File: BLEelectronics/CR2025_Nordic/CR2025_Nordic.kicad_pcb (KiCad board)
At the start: 2 copper layers, 40.7 x 31.3 mm, 35 parts, among them IC1 LTC4412xS6, IC2 PCF8523T, IC3 MX25R6435FM2IL0, IC4 LTC4054LES5-4.2#TRPBF, J1 Nordic_nRF52840_breakout, J4 Conn_01x01_Female, Q1 Si2307CDS, Q2 Si7463DP, U1 LP5907MFX-3.3, U2 BAT-HLD-001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

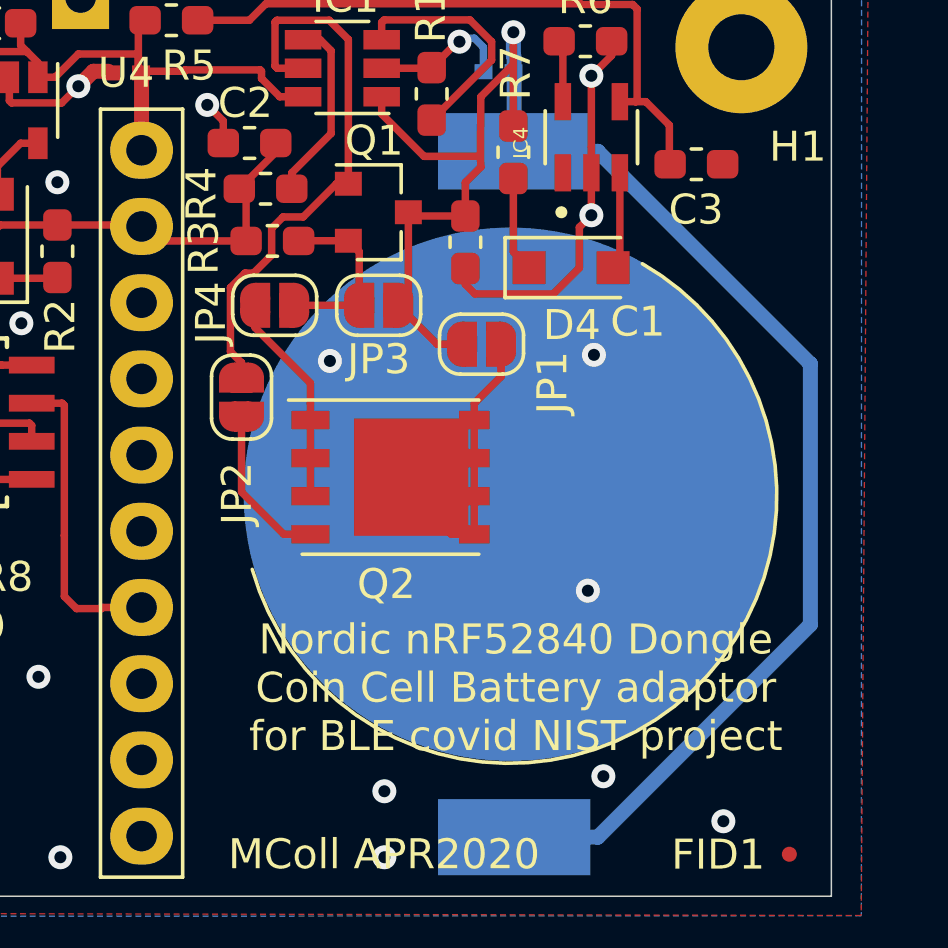
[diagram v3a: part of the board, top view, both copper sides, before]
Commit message: Expensive samsung capacitor removed
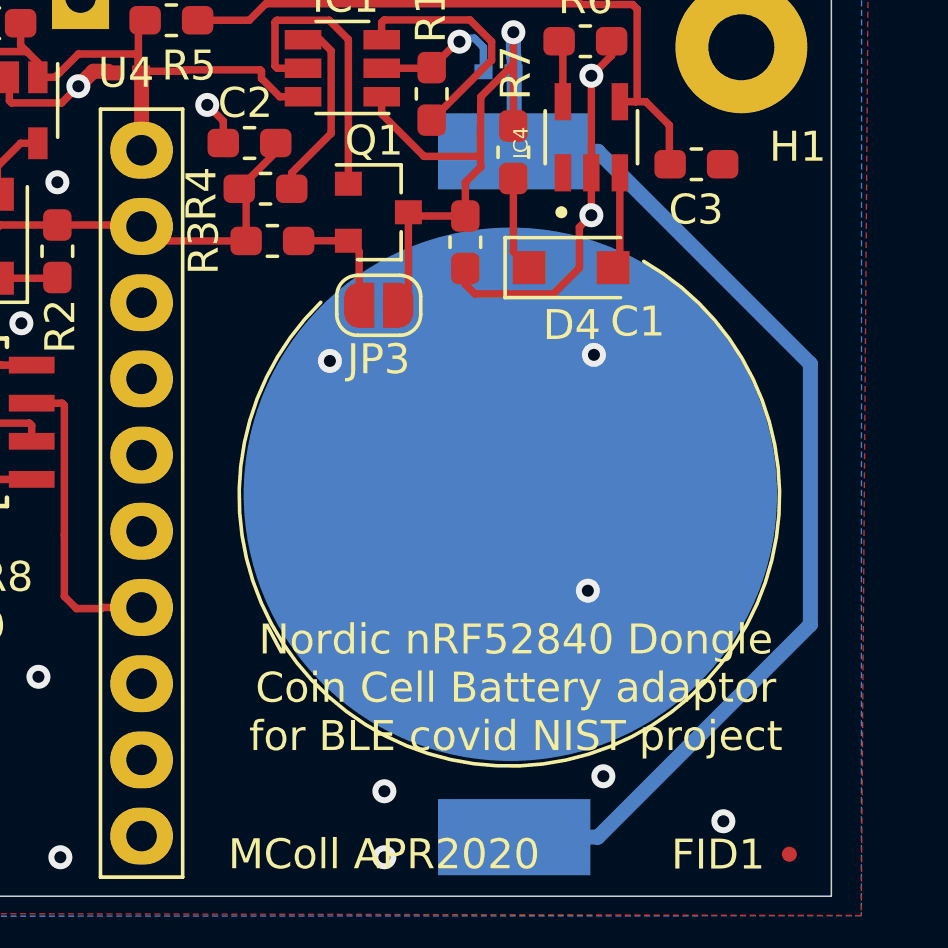
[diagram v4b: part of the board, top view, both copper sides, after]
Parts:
- removed JP1, JP2, JP4: Jumper_2_Open, Jumper:SolderJumper-2_P1.3mm_Open_RoundedPad1.0x1.5mm
- removed Q2: Si7463DP, Package_SO:PowerPAK_SO-8_Single
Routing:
- net Net-(JP1-Pad1): track 9.93 -> 0.00 mm
- net Net-(IC1-Pad5): track 19.0 -> 9.97 mm
- net Net-(JP4-Pad1): track 7.13 -> 0.00 mm
- net Net-(JP2-Pad2): track 5.39 -> 0.00 mm
- net /3V: track 59.7 -> 57.1 mm
- net Net-(JP3-Pad2): track 6.13 -> 3.96 mm

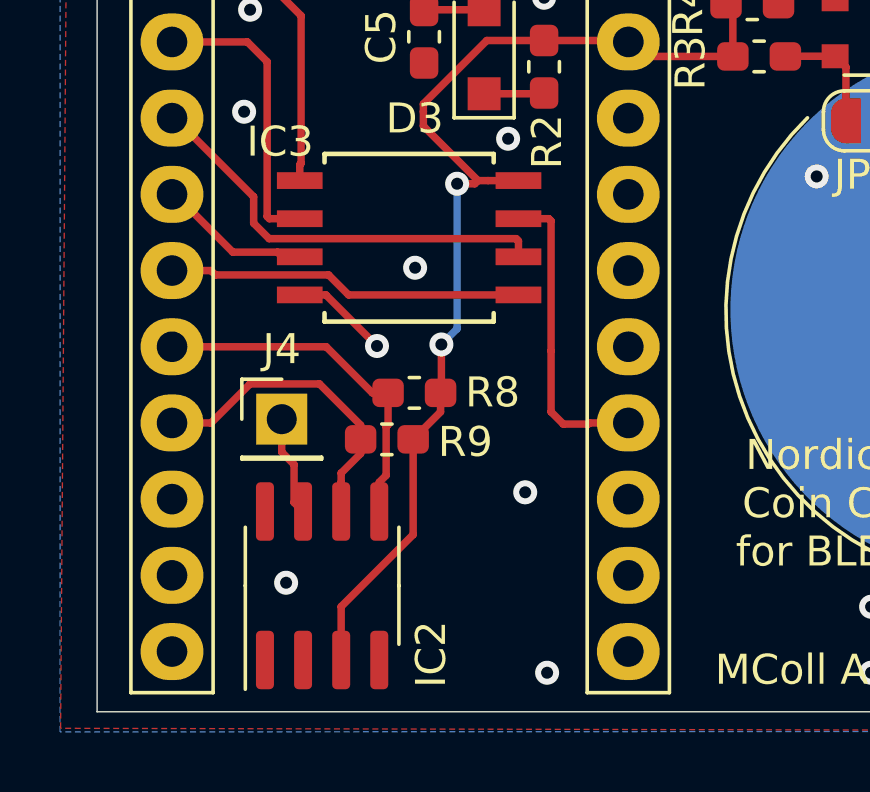
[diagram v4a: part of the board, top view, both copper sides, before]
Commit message: Moved power from pin 3 VBat to pin 8 Vdd on RTC. Swapped SIO3 and SDA on 1a and 1b. Changed battery footprint to allow backside routing for Flash and USB data. Todo: Unbreak MVP1B layout rerouting.
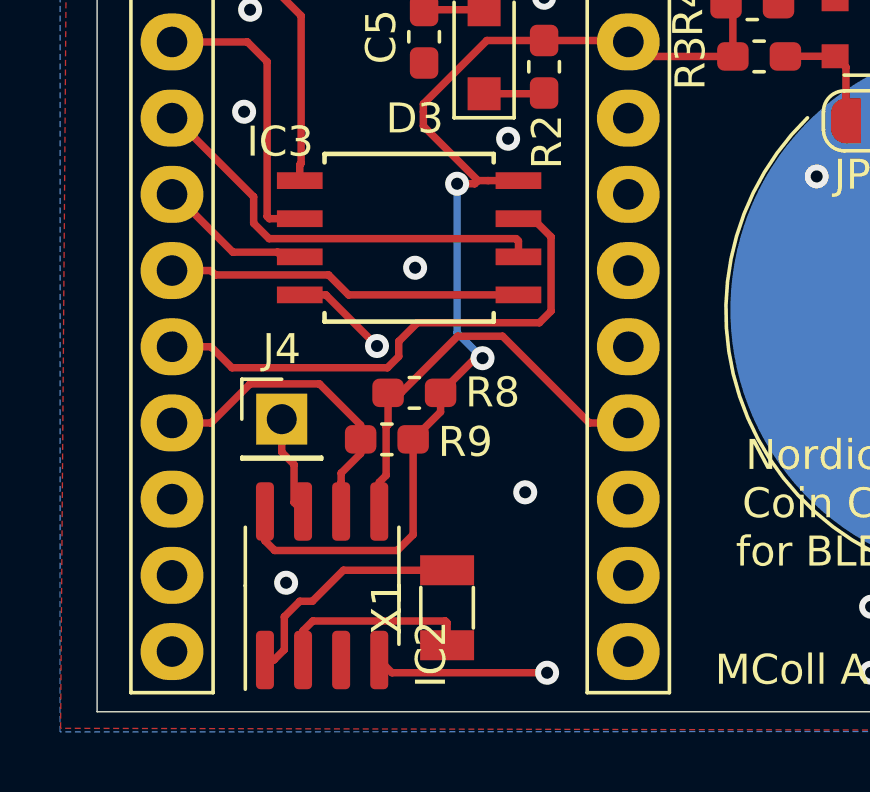
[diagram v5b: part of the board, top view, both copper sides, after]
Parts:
- added X1: 32.768KHZ, Crystal:Crystal_SMD_3215-2Pin_3.2x1.5mm, F.Cu at (136.0, 100.5)
- R8, R9: value 4.7K -> 10K
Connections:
- IC2 pad 3: /VDD_3V -> Net-(IC2-Pad3)
- IC2 pad 8: Net-(IC2-Pad8) -> /VDD_3V
- J1 pad 14: /RESET -> /SDA
- J1 pad 6: /SDA -> /RESET
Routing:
- net Net-(IC2-Pad1): track 0.00 -> 7.95 mm
- net /RESET: track 10.3 -> 17.9 mm
- net Net-(IC2-Pad2): track 0.00 -> 6.68 mm
- net GND: track 26.9 -> 32.6 mm
- net /SDA: track 12.0 -> 14.1 mm
- net /VDD_3V: track 38.2 -> 40.2 mm

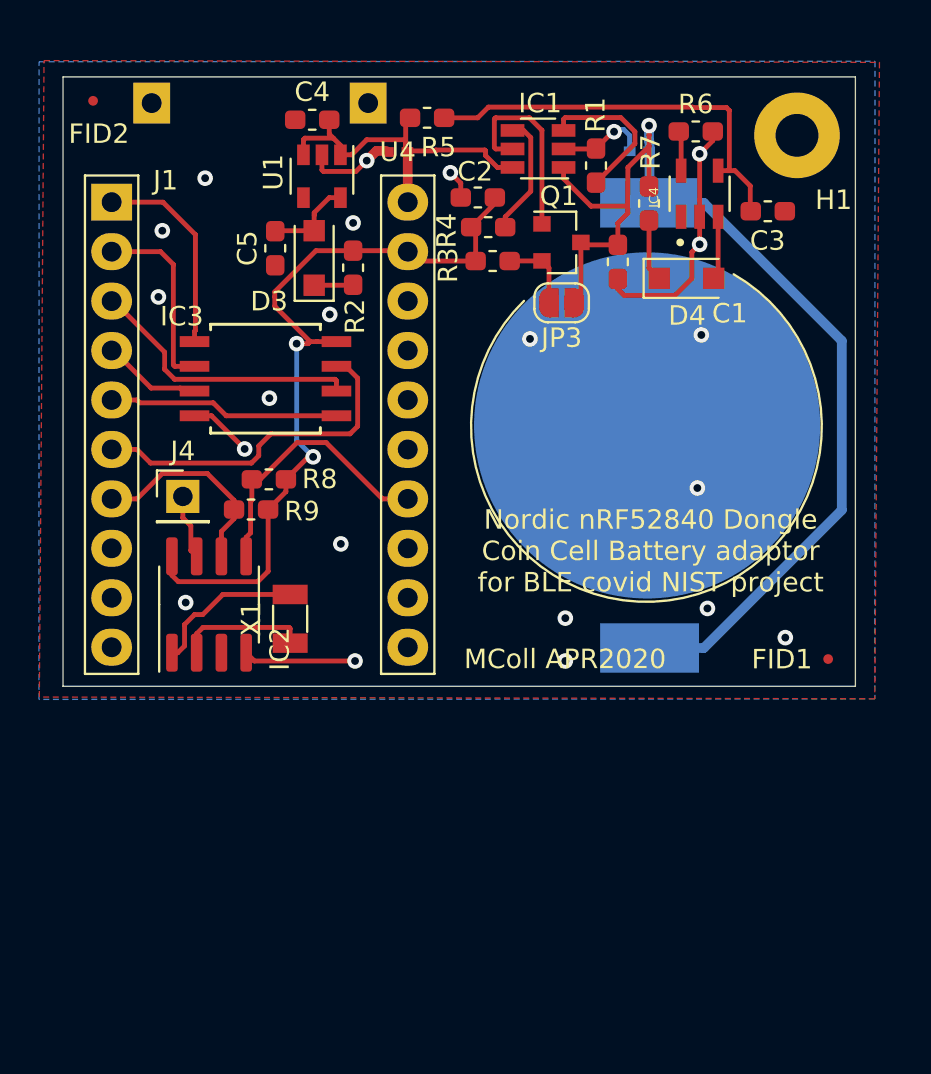
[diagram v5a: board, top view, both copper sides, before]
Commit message: refactored the MVP 1a to single sided form factor.
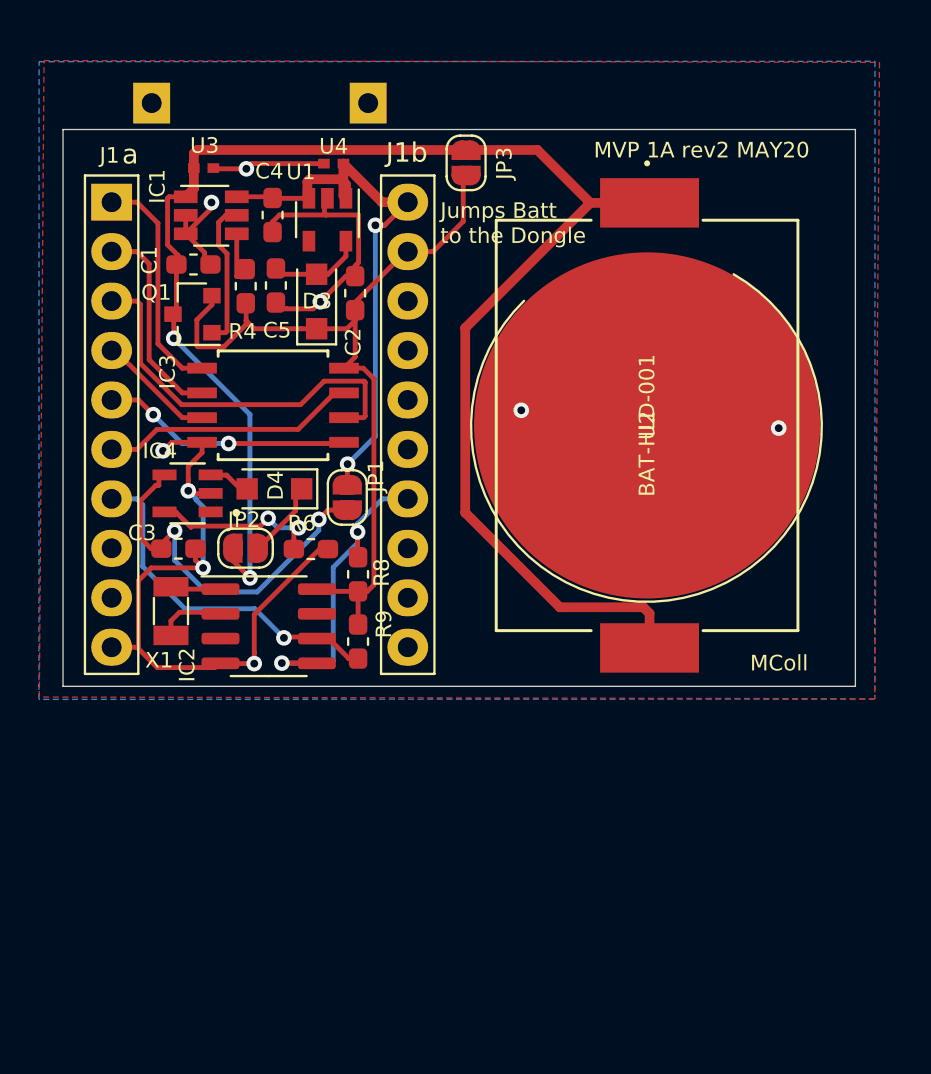
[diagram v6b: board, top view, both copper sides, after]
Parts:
- removed FID1, FID2: Fiducial, Fiducial:Fiducial_0.5mm_Mask1mm
- removed H1: MountingHole, MountingHole:MountingHole_2.2mm_M2_Pad
- removed J4: Conn_01x01_Female, Connector_PinHeader_2.54mm:PinHeader_1x01_P2.54mm_Vertical
- removed R1, R2, R3, R5, R7: 0, Resistor_SMD:R_0603_1608Metric_Pad1.05x0.95mm_HandSolder
- added JP1: Jumper_2_Open, Jumper:SolderJumper-2_P1.3mm_Open_RoundedPad1.0x1.5mm, F.Cu at (138.9, 94.3)
- added JP2: Jumper_2_Open, Jumper:SolderJumper-2_P1.3mm_Open_RoundedPad1.0x1.5mm, F.Cu at (133.7, 96.9)
- U2, U3: moved to F.Cu
- moved C3 34.9 mm to (130.2, 96.9)
- moved IC4 30.5 mm to (130.7, 94.1), turned to 180 degrees
- moved R6 29.2 mm to (137.0, 97.0)
- moved D4 23.8 mm to (135.2, 93.9), turned to 180 degrees
- moved U3 22.4 mm to (131.5, 77.4), turned to 180 degrees
- moved C1 21.8 mm to (131.0, 82.3), turned to 0 degrees
- moved Q1 19.3 mm to (130.9, 84.9), turned to 180 degrees
- moved IC1 17.1 mm to (131.9, 79.8), turned to 0 degrees
- moved R4 12.8 mm to (133.7, 83.4), turned to 90 degrees
- moved R9 8.73 mm to (139.5, 101.7), turned to 270 degrees
- moved JP3 8.70 mm to (145.0, 77.1), turned to 270 degrees
- moved C2 7.99 mm to (139.3, 83.8), turned to 90 degrees
- moved R8 6.69 mm to (139.5, 98.2), turned to 90 degrees
- moved X1 6.13 mm to (129.8, 100.1)
- moved C4 5.30 mm to (135.1, 79.8), turned to 90 degrees
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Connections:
- D3 pad 1: Net-(D3-Pad1) -> /VDD_3V
- IC1 pad 3: Net-(IC1-Pad3) -> GND
- JP3 pad 2: Net-(JP3-Pad2) -> /VDD_3V
- Q1 pad 2: Net-(JP3-Pad2) -> /VDD_3V
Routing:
- net GND: track 32.6 -> 59.4 mm, vias 22 -> 9
- net /3V: track 57.1 -> 83.3 mm, vias 1 -> 2
- net /5Vusb: track 19.1 -> 30.3 mm, vias 0 -> 2
- net Net-(IC1-Pad3): track 8.02 -> 0.00 mm
- net Net-(IC4-Pad5): track 1.80 -> 9.56 mm, vias 0 -> 2
- net /SCL: track 10.5 -> 18.0 mm, vias 0 -> 1
- net /SCLK: track 14.3 -> 20.4 mm
- net Net-(IC2-Pad1): track 7.95 -> 2.65 mm
- net /RESET: track 17.9 -> 13.2 mm
- net Net-(JP3-Pad2): track 3.96 -> 0.00 mm
- net Net-(IC1-Pad4): track 6.23 -> 2.67 mm
- net /VDD_3V: track 40.2 -> 43.7 mm, vias 2 -> 0
- net Net-(IC2-Pad7): track 3.37 -> 0.00 mm
- net Net-(IC2-Pad2): track 6.68 -> 3.48 mm
- net /SDA: track 14.1 -> 16.6 mm, vias 0 -> 2
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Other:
- board size 40.7 x 31.3 mm -> 40.7 x 28.6 mm
- board text added: "J1b"
- board text added: "Jumps Batt to the Dongle"
- board text added: "MColl"
- board text added: "MVP 1A rev2 MAY20"
- board text added: "a"
- board text removed: "MColl APR2020"
- board text removed: "Nordic nRF52840 Dongle Coin Cell Battery adaptor for BLE covid NIST project"

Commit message: generated gerber files for JLC order 07MAy20 of MVP-1a-rev2
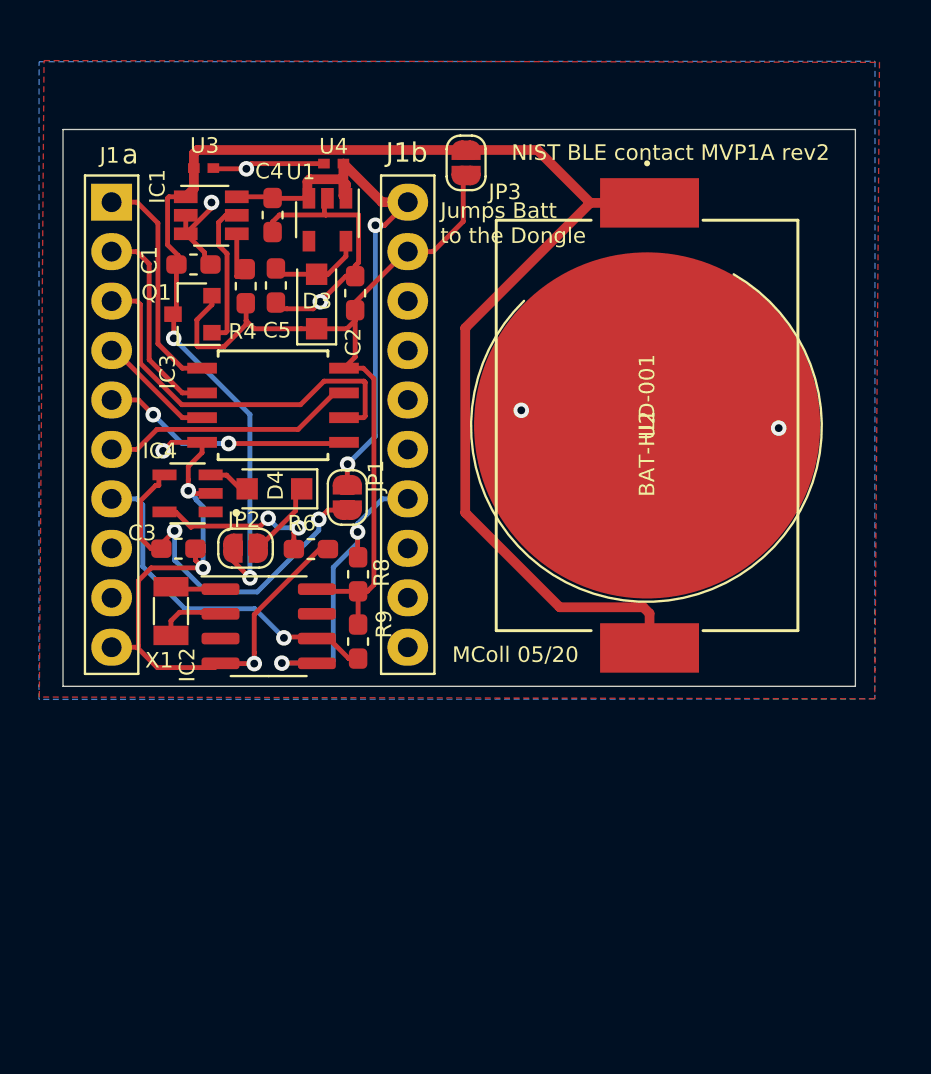
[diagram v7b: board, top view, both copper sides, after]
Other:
- board text added: "MColl 05/20"
- board text added: "NIST BLE contact MVP1A rev2"
- board text removed: "MColl"
- board text removed: "MVP 1A rev2 MAY20"
